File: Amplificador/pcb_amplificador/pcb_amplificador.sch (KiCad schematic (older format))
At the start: 124 parts, among them CON1 SJ-3523-SMT-TR, J1 Screw_Terminal_01x02, J2 Conn_01x03_Male, J3 Screw_Terminal_01x06, K1 SANYOU_SRD_Form_B, M1 FDS9934C, M2 FDS9934C, M3 FDS9934C, Q1 BC860, Q10 BD139, Q11 BD140, Q12 BD139, Q13 2SA1943-O_Q_, Q14 2SC5200-O_Q, Q15 2SA1943-O_Q_, Q16 2SC5200-O_Q, Q17 2SAR514P5, Q18 BC860, Q19 BC860, Q2 BC860, Q20 2SAR514P5, Q21 2SCR514P5, Q22 2SCR514P5, Q23 2SCR514P5, Q24 2SAR514P5, Q25 2SCR514P5, Q26 BC817, Q27 BC817, Q28 BC807, Q3 BC850, Q4 BC850, Q5 BC860, Q6 BC860, Q7 BC850, Q8 2SCR514P5, Q9 2SCR514P5

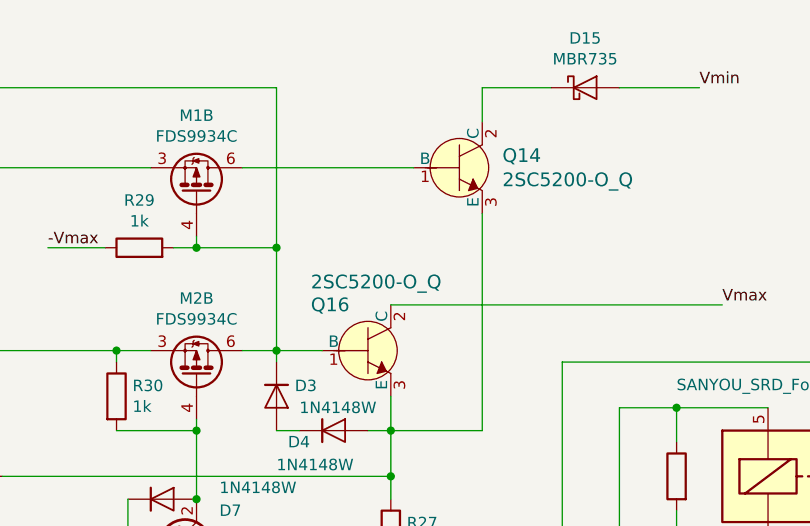
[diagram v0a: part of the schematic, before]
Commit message: Modificacion del modelo de los transistores de salida y cambios a algunos capacitores de filtrado del circuito; actualización de las especificaciones y agregado de diagramas.
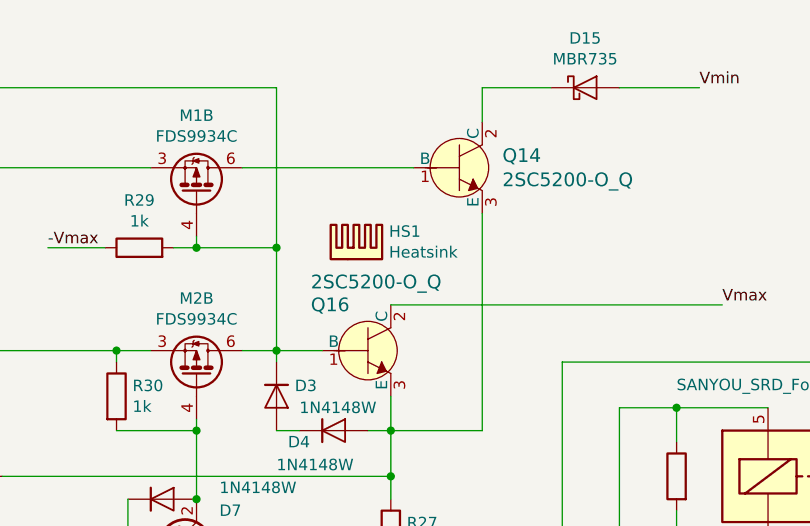
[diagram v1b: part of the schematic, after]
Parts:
- added HS1: Heatsink, symbol Mechanical:Heatsink
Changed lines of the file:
@@
 Wire Wire Line
 	4150 4650 4150 5250
+$Comp
+L Mechanical:Heatsink HS1
+U 1 1 5D0AD5E3
+P 8200 1550
+F 0 "HS1" H 8342 1671 50  0000 L CNN
+F 1 "Heatsink" H 8342 1580 50  0000 L CNN
+F 2 "" H 8212 1550 50  0001 C CNN
+F 3 "" H 8212 1550 50  0001 C CNN
+	1    8200 1550
+	1    0    0    -1
+$EndComp
 $EndSCHEMATC
